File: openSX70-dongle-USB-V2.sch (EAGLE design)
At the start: 25 parts, among them J1 687106183722, J2 SJ-3523-SMT-TR, U1 FT232RLSSOP

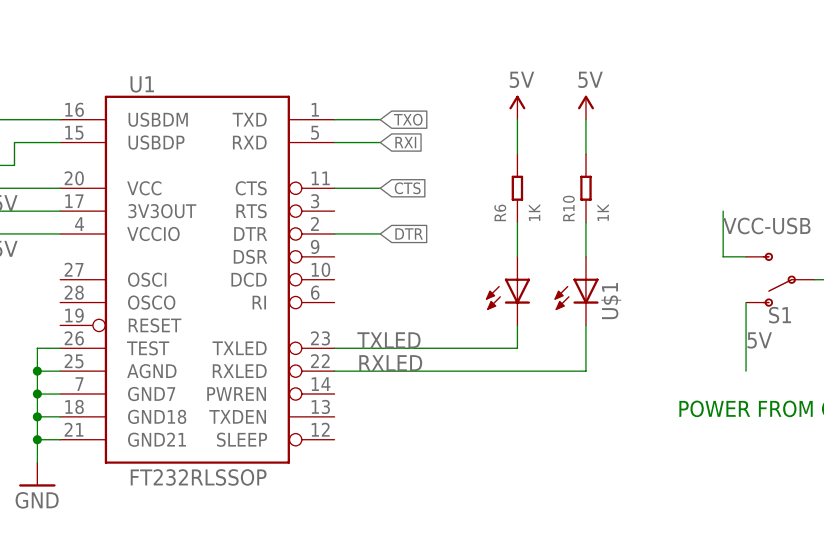
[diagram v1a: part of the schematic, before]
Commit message: fixed dual led footprint
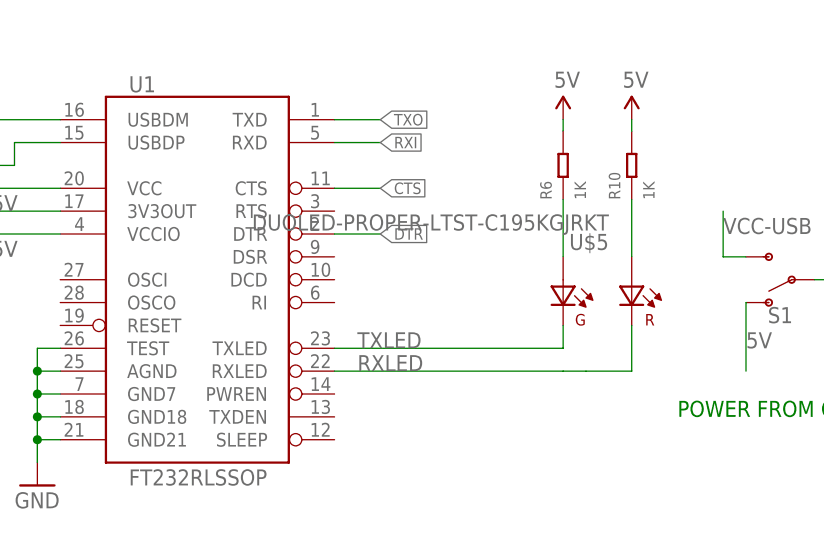
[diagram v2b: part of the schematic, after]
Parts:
- removed U$1: DUAL-LED-0603-BIS, _openSX70:DUAL-LED-0603-BIS
- added U$5: DUOLED-PROPER-LTST-C195KGJRKT, _openSX70:DUOLED-PROPER-LTST-C195KGJRKT
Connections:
- net N$14: now also R6.1, U$5.A1; no longer R10.1, U$1.A1
- net N$9: now also R10.1, U$5.A2; no longer R6.1, U$1.A
- net RXLED: now also U$5.K2; no longer U$1.C1
- net TXLED: now also U$5.K1; no longer U$1.C
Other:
- moved on the sheet: R10, R6
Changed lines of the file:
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@@
 <part name="GND3" library="SparkFun" deviceset="GND" device=""/>
 <part name="J1" library="openSX70_PATHFINDER_V5.5-SEEED_20180522" deviceset="687106183722" device=""/>
-<part name="S1" library="SparkFun-Switches" library_urn="urn:adsk.eagle:library:535" deviceset="SWITCH-SPDT" device="-SMD-RIGHT-ANGLE" package3d_urn="urn:adsk.eagle:package:40179/1"/>
-<part name="U$1" library="_openSX70" deviceset="DUAL-LED-0603-BIS" device=""/>
+<part name="S1" library="SparkFun-Switches" deviceset="SWITCH-SPDT" device="-SMD-RIGHT-ANGLE"/>
 <part name="GND-ISO2" library="supply2" library_urn="urn:adsk.eagle:library:372" deviceset="GND" device=""/>
-<part name="S2" library="SparkFun-Switches" library_urn="urn:adsk.eagle:library:535" deviceset="SWITCH-SPDT" device="-SMD-RIGHT-ANGLE" package3d_urn="urn:adsk.eagle:package:40179/1"/>
-<part name="S3" library="SparkFun-Switches" library_urn="urn:adsk.eagle:library:535" deviceset="SWITCH-SPDT" device="-SMD-RIGHT-ANGLE" package3d_urn="urn:adsk.eagle:package:40179/1"/>
+<part name="S2" library="SparkFun-Switches" deviceset="SWITCH-SPDT" device="-SMD-RIGHT-ANGLE"/>
+<part name="S3" library="SparkFun-Switches" deviceset="SWITCH-SPDT" device="-SMD-RIGHT-ANGLE"/>
 <part name="J2" library="SJ-3523-SMT-TR" deviceset="SJ-3523-SMT-TR" device=""/>
 <part name="D1" library="Seeed-LED-2016" deviceset="SMD-LED-CLEAR-YELLOW(0805)" device="" value="YELLOW-0805"/>
+<part name="U$5" library="_openSX70" deviceset="DUOLED-PROPER-LTST-C195KGJRKT" device=""/>
 </parts>
 <sheets>
@@
 <attribute name="VALUE" x="88.9" y="124.46" size="1.778" layer="96"/>
 </instance>
-<instance part="R6" gate="G$1" x="175.26" y="144.78" rot="R90">
-<attribute name="NAME" x="173.99" y="140.97" size="1.27" layer="95" ratio="10" rot="R90"/>
-<attribute name="VALUE" x="177.8" y="140.97" size="1.27" layer="96" ratio="10" rot="R90"/>
-</instance>
-<instance part="R10" gate="G$1" x="182.88" y="144.78" rot="R90">
-<attribute name="NAME" x="181.61" y="140.97" size="1.27" layer="95" ratio="10" rot="R90"/>
-<attribute name="VALUE" x="185.42" y="140.97" size="1.27" layer="96" ratio="10" rot="R90"/>
-</instance>
-<instance part="U$2" gate="G$1" x="175.26" y="152.4">
-<attribute name="VALUE" x="174.244" y="155.956" size="1.778" layer="96"/>
+<instance part="R6" gate="G$1" x="180.34" y="147.32" rot="R90">
+<attribute name="NAME" x="179.07" y="143.51" size="1.27" layer="95" ratio="10" rot="R90"/>
+<attribute name="VALUE" x="182.88" y="143.51" size="1.27" layer="96" ratio="10" rot="R90"/>
+</instance>
+<instance part="R10" gate="G$1" x="187.96" y="147.32" rot="R90">
+<attribute name="NAME" x="186.69" y="143.51" size="1.27" layer="95" ratio="10" rot="R90"/>
+<attribute name="VALUE" x="190.5" y="143.51" size="1.27" layer="96" ratio="10" rot="R90"/>
+</instance>
+<instance part="U$2" gate="G$1" x="180.34" y="152.4">
+<attribute name="VALUE" x="179.324" y="155.956" size="1.778" layer="96"/>
 </instance>
 <instance part="U$3" gate="G$1" x="109.22" y="157.48">
 <attribute name="VALUE" x="108.204" y="161.036" size="1.778" layer="96"/>
 </instance>
-<instance part="U$4" gate="G$1" x="182.88" y="152.4">
-<attribute name="VALUE" x="181.864" y="155.956" size="1.778" layer="96"/>
+<instance part="U$4" gate="G$1" x="187.96" y="152.4">
+<attribute name="VALUE" x="186.944" y="155.956" size="1.778" layer="96"/>
 </instance>
 <instance part="USB1" gate="G$1" x="43.18" y="147.32">
@@
 <attribute name="VALUE" x="204.724" y="137.922" size="1.778" layer="96" font="vector" rot="R180" align="top-center"/>
 </instance>
-<instance part="U$1" gate="G$1" x="175.26" y="134.62">
-<attribute name="NAME" x="178.816" y="130.048" size="1.778" layer="95" rot="R90"/>
-<attribute name="NAME" x="186.436" y="130.048" size="1.778" layer="95" rot="R90"/>
-</instance>
 <instance part="GND-ISO2" gate="GND" x="7.62" y="25.4" rot="R270">
 <attribute name="VALUE" x="4.445" y="27.305" size="1.778" layer="96" rot="R270"/>
@@
 <attribute name="NAME" x="38.1" y="-1.27" size="1.27" layer="95" ratio="10"/>
 <attribute name="VALUE" x="40.64" y="-7.62" size="1.27" layer="96" ratio="10"/>
+</instance>
+<instance part="U$5" gate="G$1" x="185.42" y="132.08" rot="MR0">
+<attribute name="NAME" x="185.42" y="137.92631875" size="1.779309375" layer="95" rot="MR0"/>
+<attribute name="VALUE" x="185.42" y="140.0882" size="1.7796" layer="96" rot="MR0"/>
 </instance>
 </instances>
@@
 <net name="TXLED" class="0">
 <segment>
-<wire x1="154.94" y1="127" x2="175.26" y2="127" width="0.1524" layer="91"/>
+<wire x1="154.94" y1="127" x2="180.34" y2="127" width="0.1524" layer="91"/>
 <label x="157.48" y="127" size="1.778" layer="95"/>
 <pinref part="U1" gate="G$1" pin="TXLED"/>
-<pinref part="U$1" gate="G$1" pin="C"/>
-<wire x1="175.26" y1="129.54" x2="175.26" y2="127" width="0.1524" layer="91"/>
+<pinref part="U$5" gate="G$1" pin="K1"/>
+<wire x1="180.34" y1="127" x2="180.34" y2="129.54" width="0.1524" layer="91"/>
 </segment>
 </net>
 <net name="RXLED" class="0">
 <segment>
-<wire x1="154.94" y1="124.46" x2="182.88" y2="124.46" width="0.1524" layer="91"/>
+<wire x1="154.94" y1="124.46" x2="180.34" y2="124.46" width="0.1524" layer="91"/>
 <label x="157.48" y="124.46" size="1.778" layer="95"/>
 <pinref part="U1" gate="G$1" pin="RXLED"/>
-<pinref part="U$1" gate="G$1" pin="C1"/>
-<wire x1="182.88" y1="124.46" x2="182.88" y2="129.54" width="0.1524" layer="91"/>
+<pinref part="U$5" gate="G$1" pin="K2"/>
+<wire x1="180.34" y1="124.46" x2="182.88" y2="124.46" width="0.1524" layer="91"/>
+<wire x1="187.96" y1="129.54" x2="187.96" y2="124.46" width="0.1524" layer="91"/>
+<wire x1="187.96" y1="124.46" x2="182.88" y2="124.46" width="0.1524" layer="91"/>
 </segment>
 </net>
@@
 </segment>
 <segment>
-<wire x1="175.26" y1="152.4" x2="175.26" y2="148.59" width="0.1524" layer="91"/>
+<wire x1="180.34" y1="152.4" x2="180.34" y2="151.13" width="0.1524" layer="91"/>
 <pinref part="R6" gate="G$1" pin="2"/>
 <pinref part="U$2" gate="G$1" pin="5V"/>
 </segment>
 <segment>
-<wire x1="182.88" y1="152.4" x2="182.88" y2="148.59" width="0.1524" layer="91"/>
+<wire x1="187.96" y1="152.4" x2="187.96" y2="151.13" width="0.1524" layer="91"/>
 <pinref part="R10" gate="G$1" pin="2"/>
 <pinref part="U$4" gate="G$1" pin="5V"/>
@@
 <wire x1="208.28" y1="134.62" x2="236.22" y2="134.62" width="0.1524" layer="91"/>
 <label x="213.36" y="137.16" size="1.778" layer="95"/>
-</segment>
-</net>
-<net name="N$9" class="0">
-<segment>
-<pinref part="R6" gate="G$1" pin="1"/>
-<pinref part="U$1" gate="G$1" pin="A"/>
-<wire x1="175.26" y1="140.97" x2="175.26" y2="137.16" width="0.1524" layer="91"/>
-</segment>
-</net>
-<net name="N$14" class="0">
-<segment>
-<pinref part="R10" gate="G$1" pin="1"/>
-<pinref part="U$1" gate="G$1" pin="A1"/>
-<wire x1="182.88" y1="140.97" x2="182.88" y2="137.16" width="0.1524" layer="91"/>
 </segment>
 </net>
@@
 </segment>
 </net>
+<net name="N$9" class="0">
+<segment>
+<pinref part="R10" gate="G$1" pin="1"/>
+<pinref part="U$5" gate="G$1" pin="A2"/>
+<wire x1="187.96" y1="143.51" x2="187.96" y2="137.16" width="0.1524" layer="91"/>
+</segment>
+</net>
+<net name="N$14" class="0">
+<segment>
+<pinref part="R6" gate="G$1" pin="1"/>
+<pinref part="U$5" gate="G$1" pin="A1"/>
+<wire x1="180.34" y1="143.51" x2="180.34" y2="137.16" width="0.1524" layer="91"/>
+</segment>
+</net>

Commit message: new origami design
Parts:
- added LED1: (no value), openSX70_PATHFINDER_V5.5-SEEED_20180522:LED3MM
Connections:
- net 3V3OUT: now also LED1.A
- net N$2: now also LED1.C
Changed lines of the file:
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@@
 <part name="D1" library="Seeed-LED-2016" deviceset="SMD-LED-CLEAR-YELLOW(0805)" device="" value="YELLOW-0805"/>
 <part name="U$5" library="_openSX70" deviceset="DUOLED-PROPER-LTST-C195KGJRKT" device=""/>
+<part name="LED1" library="openSX70_PATHFINDER_V5.5-SEEED_20180522" deviceset="LED" device="3MM"/>
 </parts>
 <sheets>
@@
 <attribute name="NAME" x="185.42" y="137.92631875" size="1.779309375" layer="95" rot="MR0"/>
 <attribute name="VALUE" x="185.42" y="140.0882" size="1.7796" layer="96" rot="MR0"/>
+</instance>
+<instance part="LED1" gate="G$1" x="45.72" y="-10.16" rot="R90">
+<attribute name="NAME" x="50.292" y="-6.604" size="1.778" layer="95" rot="R180"/>
+<attribute name="VALUE" x="50.292" y="-4.445" size="1.778" layer="96" rot="R180"/>
 </instance>
 </instances>
@@
 <segment>
 <pinref part="D1" gate="G$1" pin="+"/>
+<label x="25.4" y="-5.08" size="1.778" layer="95"/>
+<pinref part="LED1" gate="G$1" pin="A"/>
 <wire x1="41.91" y1="-2.54" x2="35.56" y2="-2.54" width="0.1524" layer="91"/>
-<label x="25.4" y="-5.08" size="1.778" layer="95"/>
+<wire x1="41.91" y1="-2.54" x2="43.18" y2="-2.54" width="0.1524" layer="91"/>
+<wire x1="43.18" y1="-2.54" x2="43.18" y2="-10.16" width="0.1524" layer="91"/>
 </segment>
 </net>
@@
 <pinref part="D1" gate="G$1" pin="-"/>
 <pinref part="R9" gate="G$1" pin="2"/>
-<wire x1="49.53" y1="-2.54" x2="53.34" y2="-2.54" width="0.1524" layer="91"/>
-</segment>
-</net>
+<wire x1="49.53" y1="-2.54" x2="50.8" y2="-2.54" width="0.1524" layer="91"/>
+<pinref part="LED1" gate="G$1" pin="C"/>
+<wire x1="50.8" y1="-2.54" x2="53.34" y2="-2.54" width="0.1524" layer="91"/>
+<wire x1="50.8" y1="-10.16" x2="50.8" y2="-2.54" width="0.1524" layer="91"/>
+<junction x="50.8" y="-2.54"/>
+</segment>
+</net>
